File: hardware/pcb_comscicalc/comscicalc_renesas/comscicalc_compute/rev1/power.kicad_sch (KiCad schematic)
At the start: 46 parts

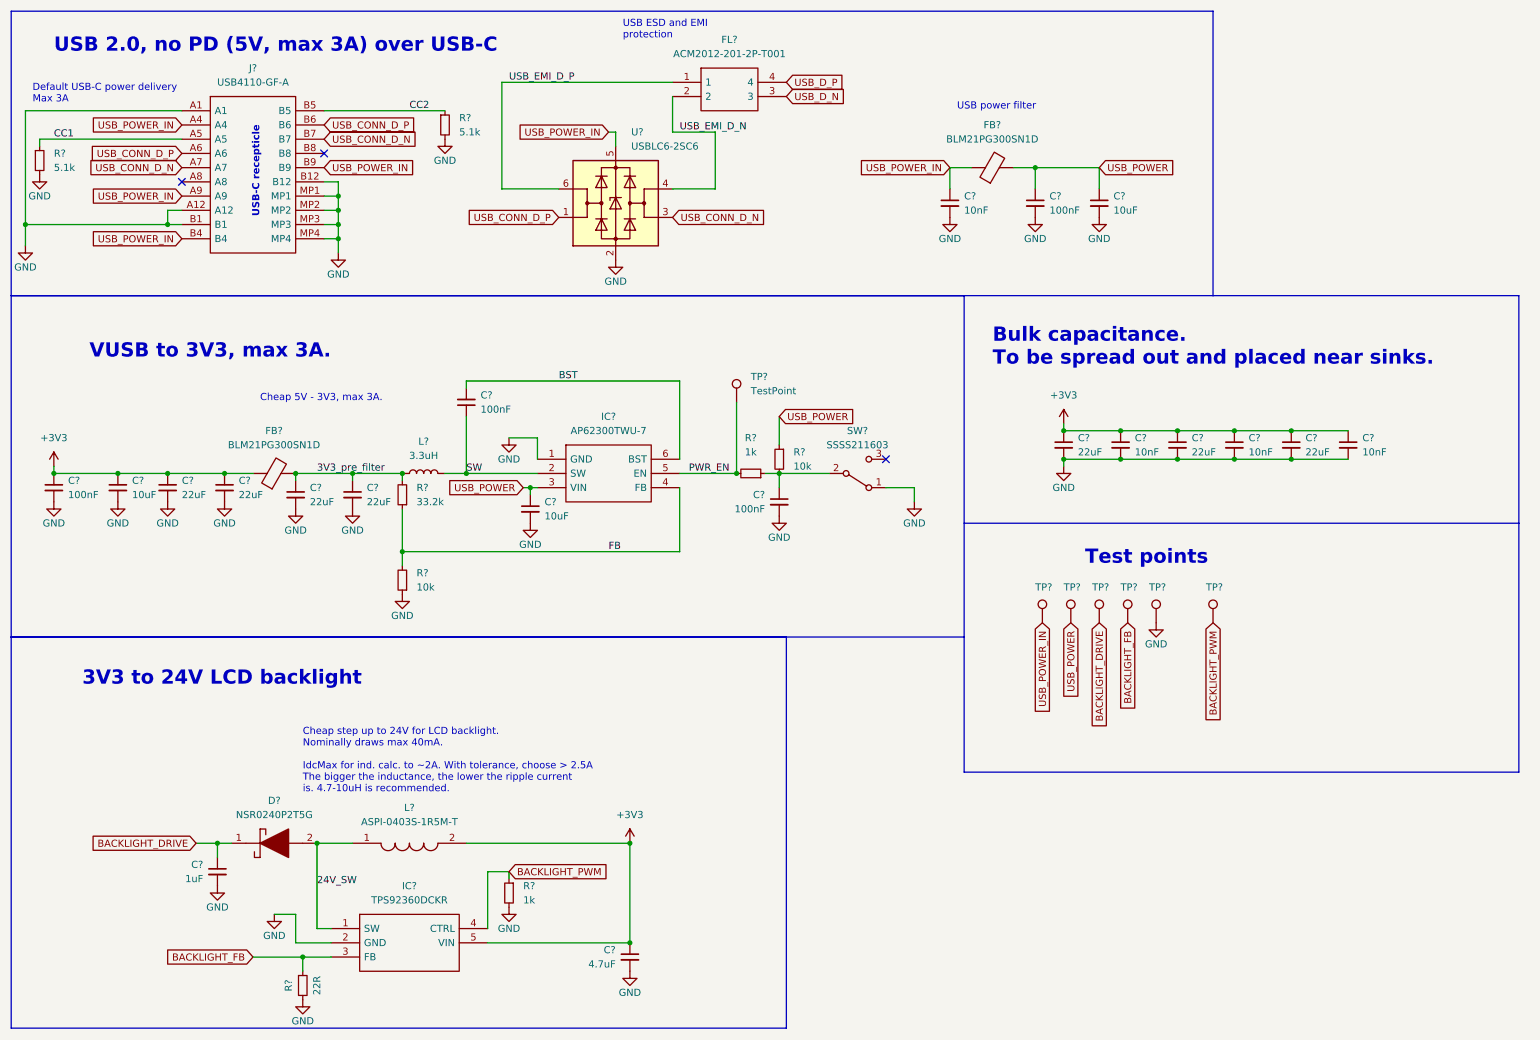
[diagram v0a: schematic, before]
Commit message: rev0 of hardware works fine with VBATT pin left open. Starting rev1 using rp2040
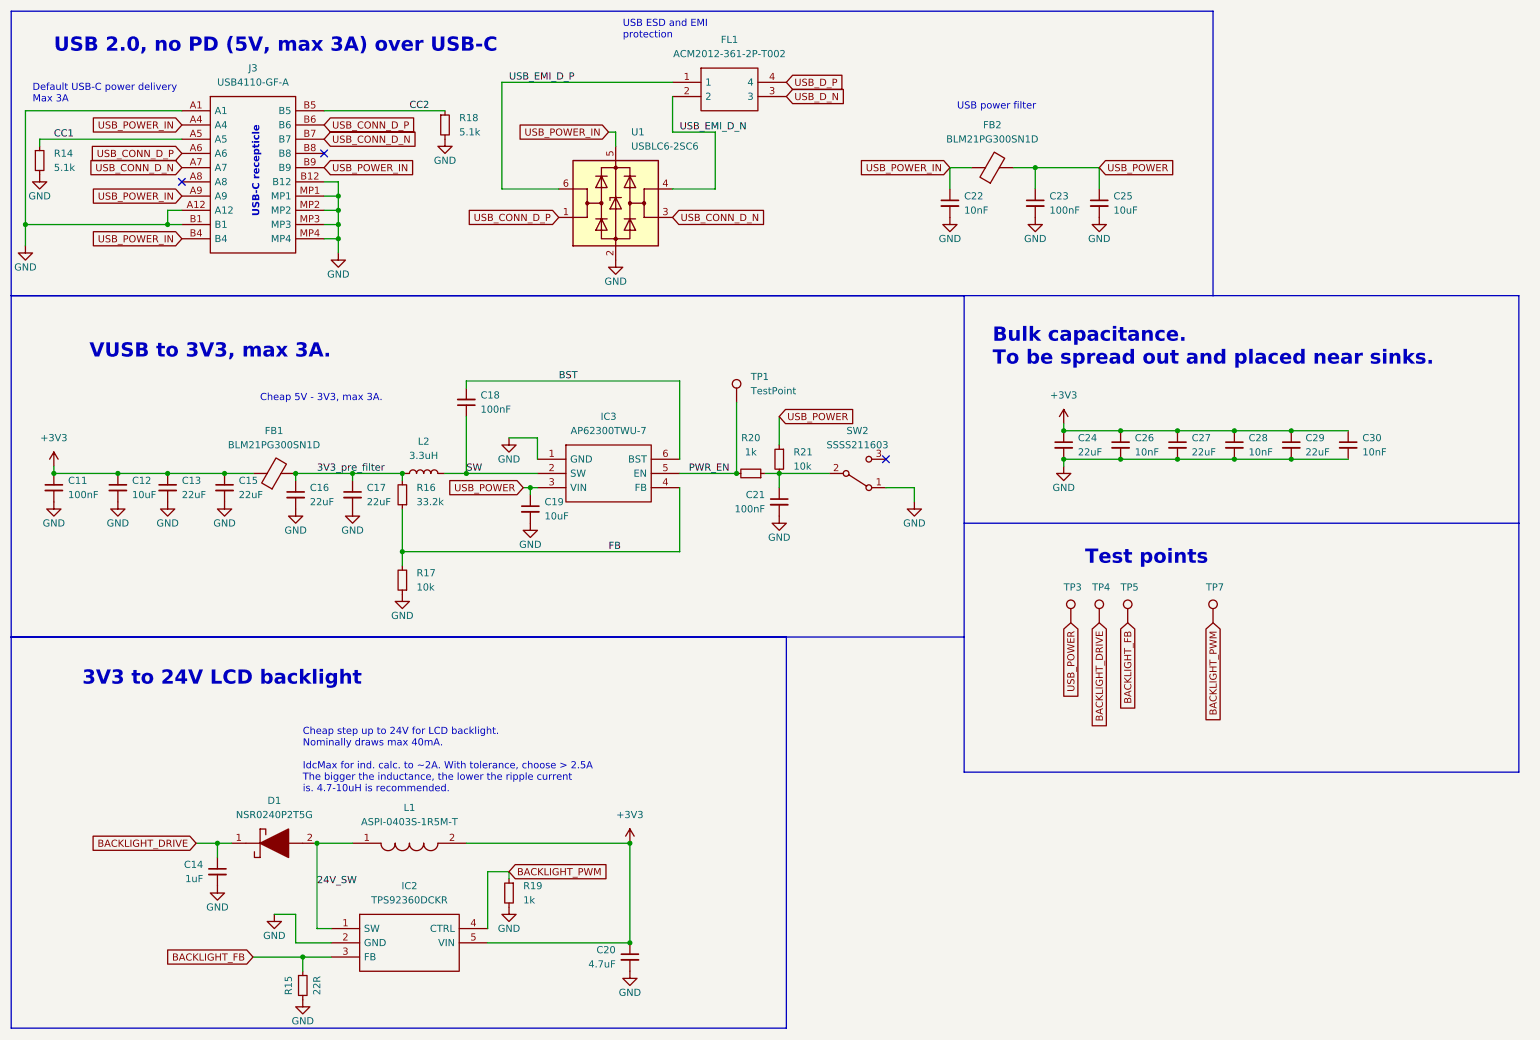
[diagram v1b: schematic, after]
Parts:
- removed TP? (x2): TestPoint, TestPoint:TestPoint_Pad_D1.5mm, symbol Connector:TestPoint
- FL1: renamed from FL?; value ACM2012-201-2P-T001 -> ACM2012-361-2P-T002; LCSC C383338 -> C87126; Manufacturer_Part_Number ACM2012-201-2P-T001 -> ACM2012-361-2P-T002; Mouser Part Number 810-ACM20122012PT001 -> 810-ACM20123612PT002
- gave numbers to parts that had none: 43
